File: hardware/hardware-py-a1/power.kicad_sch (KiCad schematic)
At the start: 24 parts, among them Q1 AO3401A, Q2 BSS138, Q3 AO3401A, Q5 AO4953A, U1 LTC4054, U2 STI3411A, U5 XC6206PxxxMR

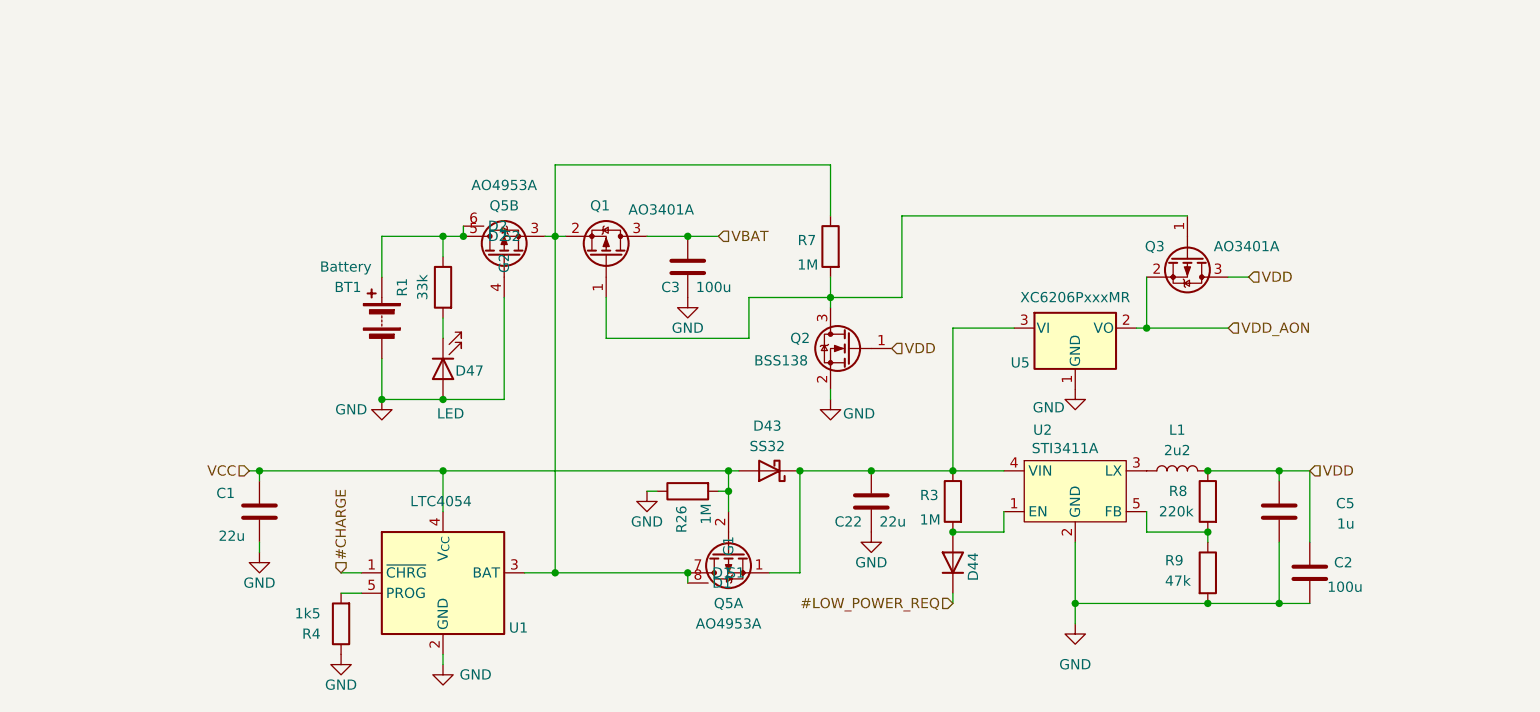
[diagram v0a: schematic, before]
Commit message: hw: pya1 schematic rearange and post assembly test for inputs
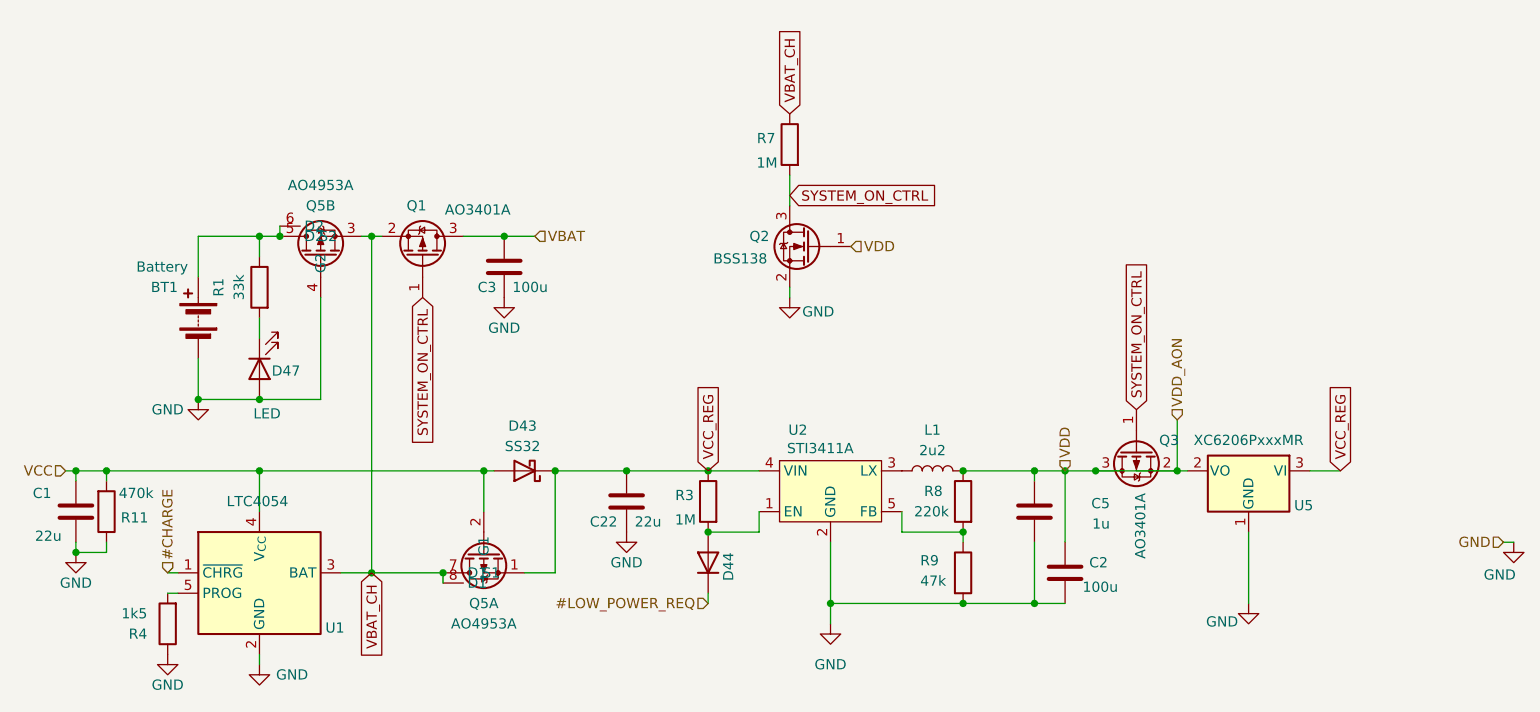
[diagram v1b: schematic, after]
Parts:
- removed R26: 1M, Resistor_SMD:R_0805_2012Metric_Pad1.20x1.40mm_HandSolder, symbol Device:R
- added R11: 470k, Resistor_SMD:R_0805_2012Metric_Pad1.20x1.40mm_HandSolder, symbol Device:R
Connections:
- net VDD_AON is gone; now on net VDD: Q3.2 (S), U5.2 (VO)
- net GND: now also R11.1
- net VCC: now also R11.2
- net VBAT_CH: now reaches Q1.2 (S), Q5.3 (S2), Q5.7 (D1), Q5.8 (D1), R7.1, U1.3 (BAT)
- net VCC_REG: now reaches C22.1, D43.1 (K), Q5.1 (S1), R3.1, U2.4 (VIN), U5.3 (VI)
- net SYSTEM_ON_CTRL: now reaches Q1.1 (G), Q2.3 (D), Q3.1 (G), R7.2
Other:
- moved on the sheet: BT1, C1, C2, C22, C3, C5, D43, D44, D47, L1, Q1, Q2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
